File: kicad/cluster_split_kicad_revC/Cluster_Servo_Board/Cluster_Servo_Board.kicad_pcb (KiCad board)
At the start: 4 copper layers, 220 x 110 mm, 39 parts, among them J1 JST_XH_8, J10 POWER_5V_HICUR, J11 POWER_5V_HICUR, J2 RJ45_Amphenol_54602-x08_Horiz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, J3 RJ45_Amphenol_54602-x08_Horiz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, J4 RJ45_Amphenol_54602-x08_Horiz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, J5 RJ45_Amphenol_54602-x08_Horiz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, J6 RJ45_Amphenol_54602-x08_Horiz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, J7 RJ45_Amphenol_54602-x08_Horiz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, J8 RJ45_Amphenol_54602-x08_Horiz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, J9 RJ45_Amphenol_54602-x08_Horiz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, U1 ADAFRUIT_PCA9685_16CH_PRODUCT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, U2 74AHCT125_DIP14

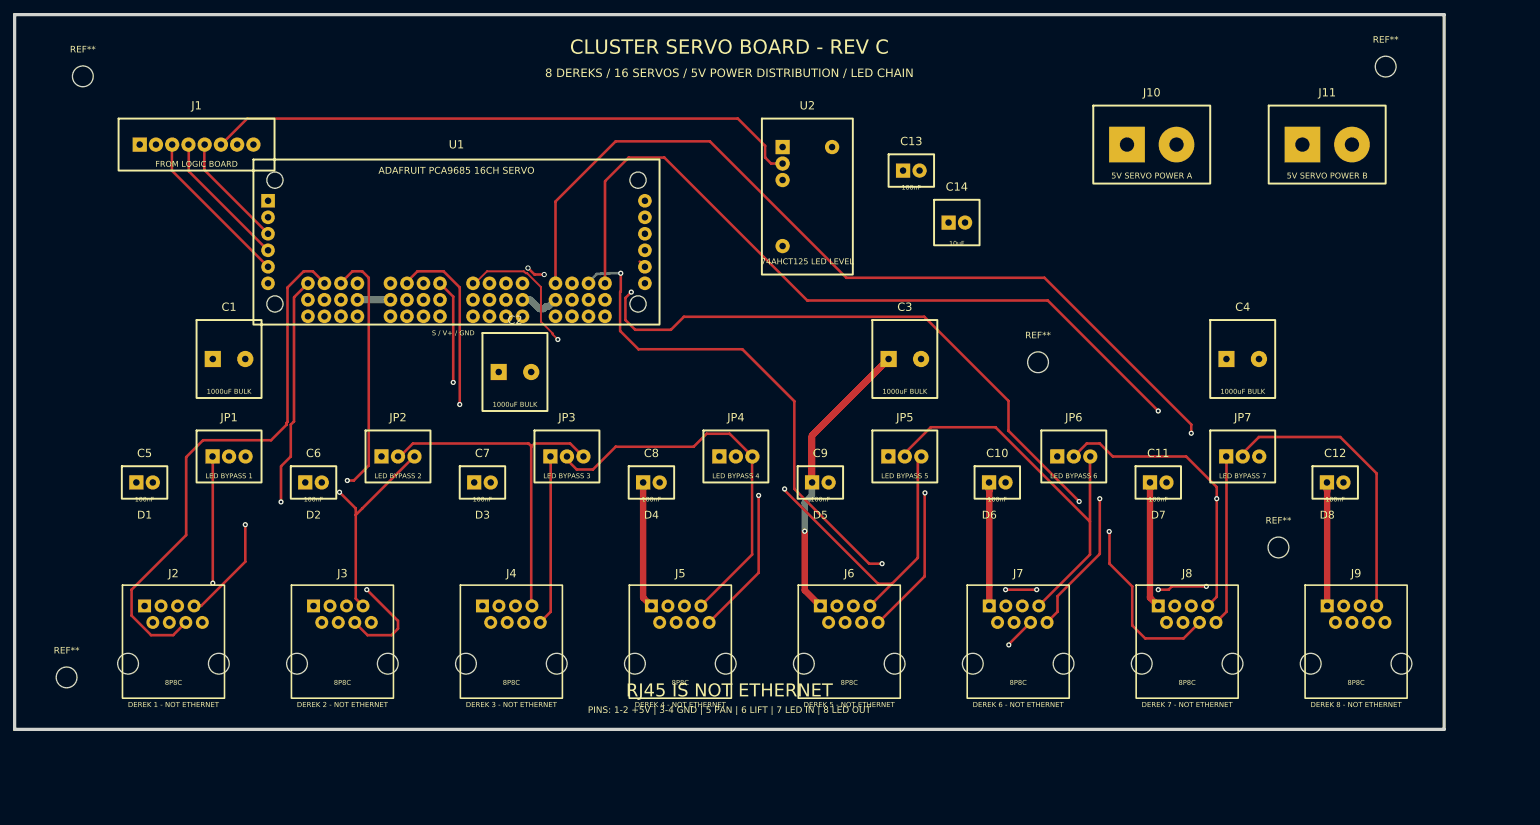
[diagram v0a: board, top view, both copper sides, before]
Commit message: Fixed RJ45 footprints on all, cleaned up routing, ready for a run at PCBWay
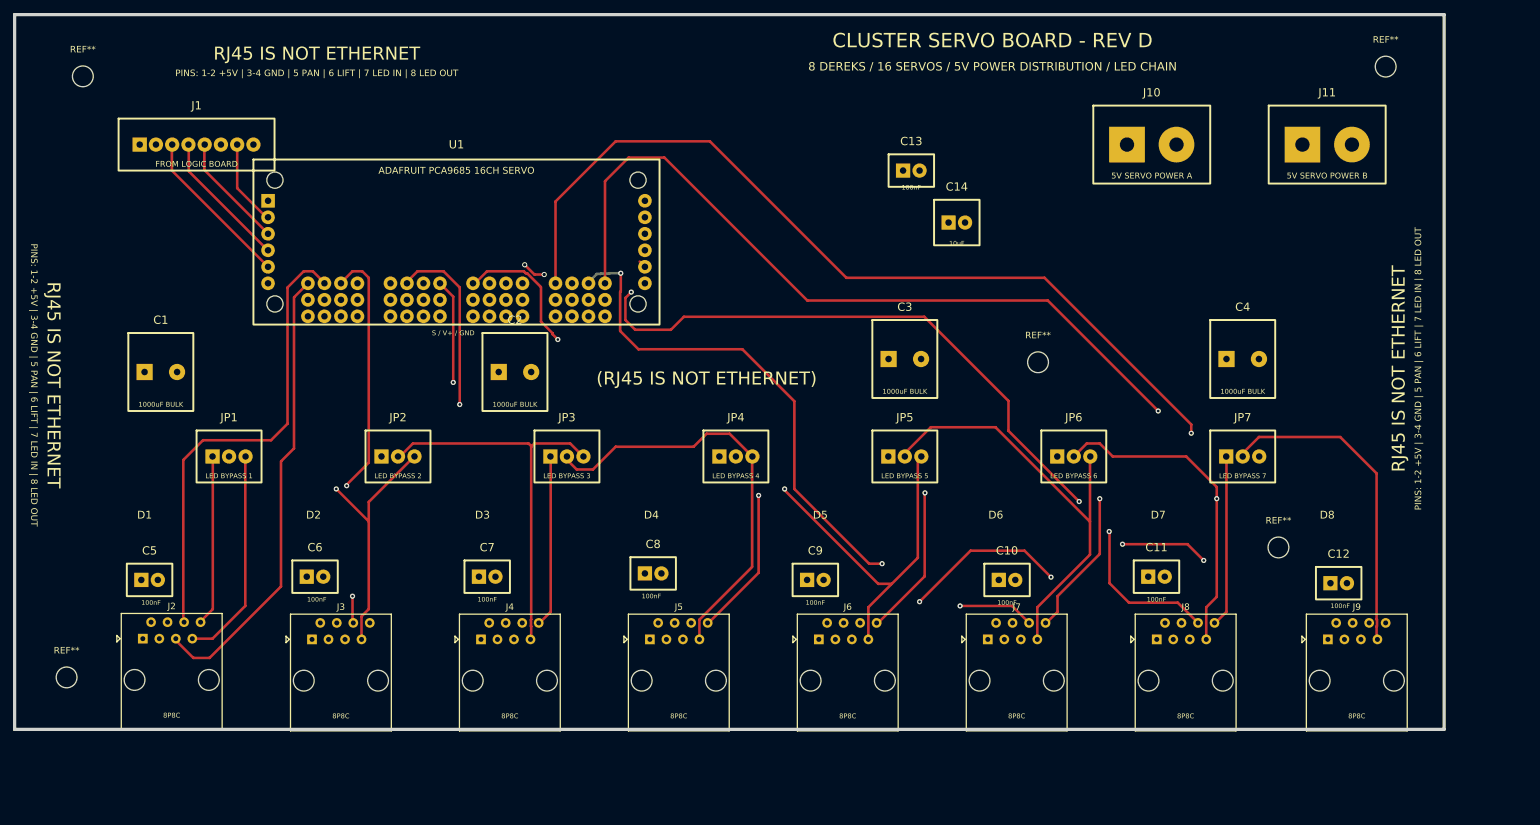
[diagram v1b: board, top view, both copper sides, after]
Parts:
- removed U2: 74AHCT125_DIP14, Custom:74AHCT125_DIP14
- moved C12 15.5 mm to (203.8, 87.5)
- moved C10 15.1 mm to (152.7, 87.0)
- moved C5 15.0 mm to (20.8, 87.0)
- moved C9 15.0 mm to (123.2, 87.0)
- moved C7 14.5 mm to (72.7, 86.5)
- moved C11 14.5 mm to (175.7, 86.5)
- moved C6 14.5 mm to (46.2, 86.5)
- moved C8 14.0 mm to (98.3, 86.0)
- moved C1 10.7 mm to (22.5, 55.0)
- moved J3 5.16 mm to (45.8, 96.2)
- moved J4 5.16 mm to (71.8, 96.2)
- moved J5 5.16 mm to (97.8, 96.2)
- moved J6 5.16 mm to (123.8, 96.2)
- moved J7 5.16 mm to (149.8, 96.2)
- moved J8 5.16 mm to (175.8, 96.2)
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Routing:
- net +5V_SERVO: track 132.6 -> 0.00 mm, vias 1 -> 0
- net LED_DATA_3V3: track 92.1 -> 0.00 mm
- net PWM10: track 104.5 -> 118.0 mm
- net PWM1: track 84.4 -> 71.9 mm
- net PWM0: track 57.9 -> 70.4 mm, vias 1 -> 0
- net PWM8: track 83.2 -> 95.1 mm
- net PWM14: track 159.9 -> 170.9 mm
- net PWM3: track 64.7 -> 54.3 mm
- net PWM5: track 75.9 -> 65.8 mm
- net PWM11: track 107.9 -> 116.7 mm
- net PWM15: track 192.4 -> 185.8 mm
- net PWM7: track 74.9 -> 81.2 mm
- net LED_IN1: track 27.8 -> 33.3 mm, vias 1 -> 0
- net PWM4: track 59.3 -> 64.7 mm
- net PWM12: track 160.2 -> 165.6 mm
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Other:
- board text added: "(RJ45 IS NOT ETHERNET)"
- board text added: "CLUSTER SERVO BOARD - REV D"
- board text removed: "CLUSTER SERVO BOARD - REV C"

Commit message: Fixed RJ45 footprints on all, cleaned up routing, ready for a run at PCBWay - more
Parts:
- added REF**: MountingHole_3.2mm_M3, MountingHole:MountingHole_3.2mm_M3, F.Cu at (89.4, 104.0)
- added REF**: MountingHole_3.2mm_M3, MountingHole:MountingHole_3.2mm_M3, F.Cu at (141.5, 104.0)
- added REF**: MountingHole_3.2mm_M3, MountingHole:MountingHole_3.2mm_M3, F.Cu at (214.5, 100.5)
- moved J9 5.84 mm to (196.3, 96.2)
- moved J8 1.93 mm to (173.8, 96.2)
- moved REF** 1.58 mm to (7.50, 100.5)
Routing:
- net PWM14: track 170.9 -> 148.1 mm
- net LED_IN8: track 49.8 -> 52.9 mm
- net LED_OUT7: track 26.2 -> 28.4 mm
- net PWM12: track 165.6 -> 167.6 mm
- net LED_IN7: track 58.9 -> 60.0 mm
- net PWM13: track 132.2 -> 131.4 mm

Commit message: Fixed servo controller footprint, submitted to JLCPCB today
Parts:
- moved J6 17.7 mm to (136.3, 108.7)
- moved C5 17.7 mm to (33.3, 99.5)
- moved C1 17.7 mm to (35.0, 67.5)
- moved C10 17.7 mm to (165.2, 99.5)
- moved C11 17.7 mm to (188.2, 99.0)
- moved C12 17.7 mm to (216.3, 100.0)
- moved C13 17.7 mm to (150.5, 36.5)
- moved C14 17.7 mm to (157.5, 44.5)
- moved C2 17.7 mm to (89.5, 67.5)
- moved C3 17.7 mm to (149.5, 65.5)
- moved C4 17.7 mm to (201.5, 65.5)
- moved C6 17.7 mm to (58.7, 99.0)
- moved C7 17.7 mm to (85.2, 99.0)
- moved C8 17.7 mm to (110.8, 98.5)
- moved J1 17.7 mm to (40.5, 32.5)
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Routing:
- net PWM13: track 131.4 -> 128.6 mm
- net PWM14: track 148.1 -> 145.5 mm
- net PWM10: track 118.0 -> 116.0 mm
- net PWM9: track 109.7 -> 107.7 mm, vias 2 -> 1
- net PWM8: track 95.1 -> 97.1 mm
- net PWM12: track 167.6 -> 166.8 mm
- net PWM11: track 116.7 -> 116.0 mm
- net PWM2: track 62.7 -> 63.2 mm
- net PWM15: track 185.4 -> 184.9 mm
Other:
- board text added: "CLUSTER SERVO BOARD - REV F"
- board text removed: "CLUSTER SERVO BOARD - REV D"
